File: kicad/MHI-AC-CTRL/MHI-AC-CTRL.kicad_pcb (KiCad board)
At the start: 2 copper layers, 51.6 x 26.8 mm, 8 parts, among them J1 Conn_01x05, U1 TSR_1-2450, U2 ESP-C3-32S-Kit, U3 LEVEL-SHIFTER-4CH

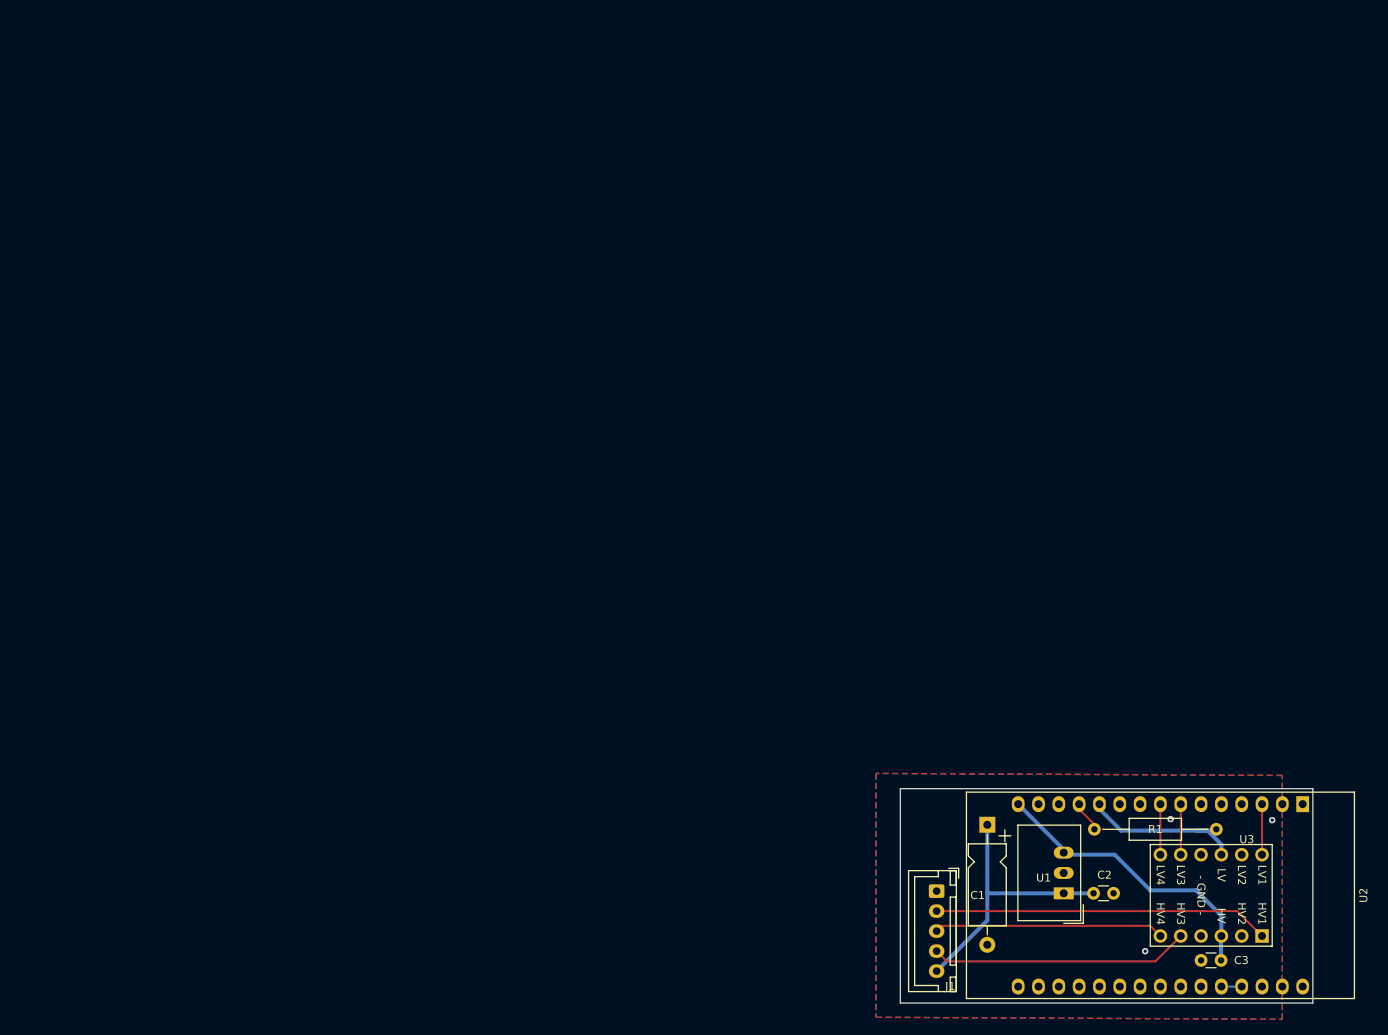
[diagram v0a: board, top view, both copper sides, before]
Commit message: Custom Version for ESP32-C3-DevkitM-1
Custom Version for ESP32-C3-DevkitM-1
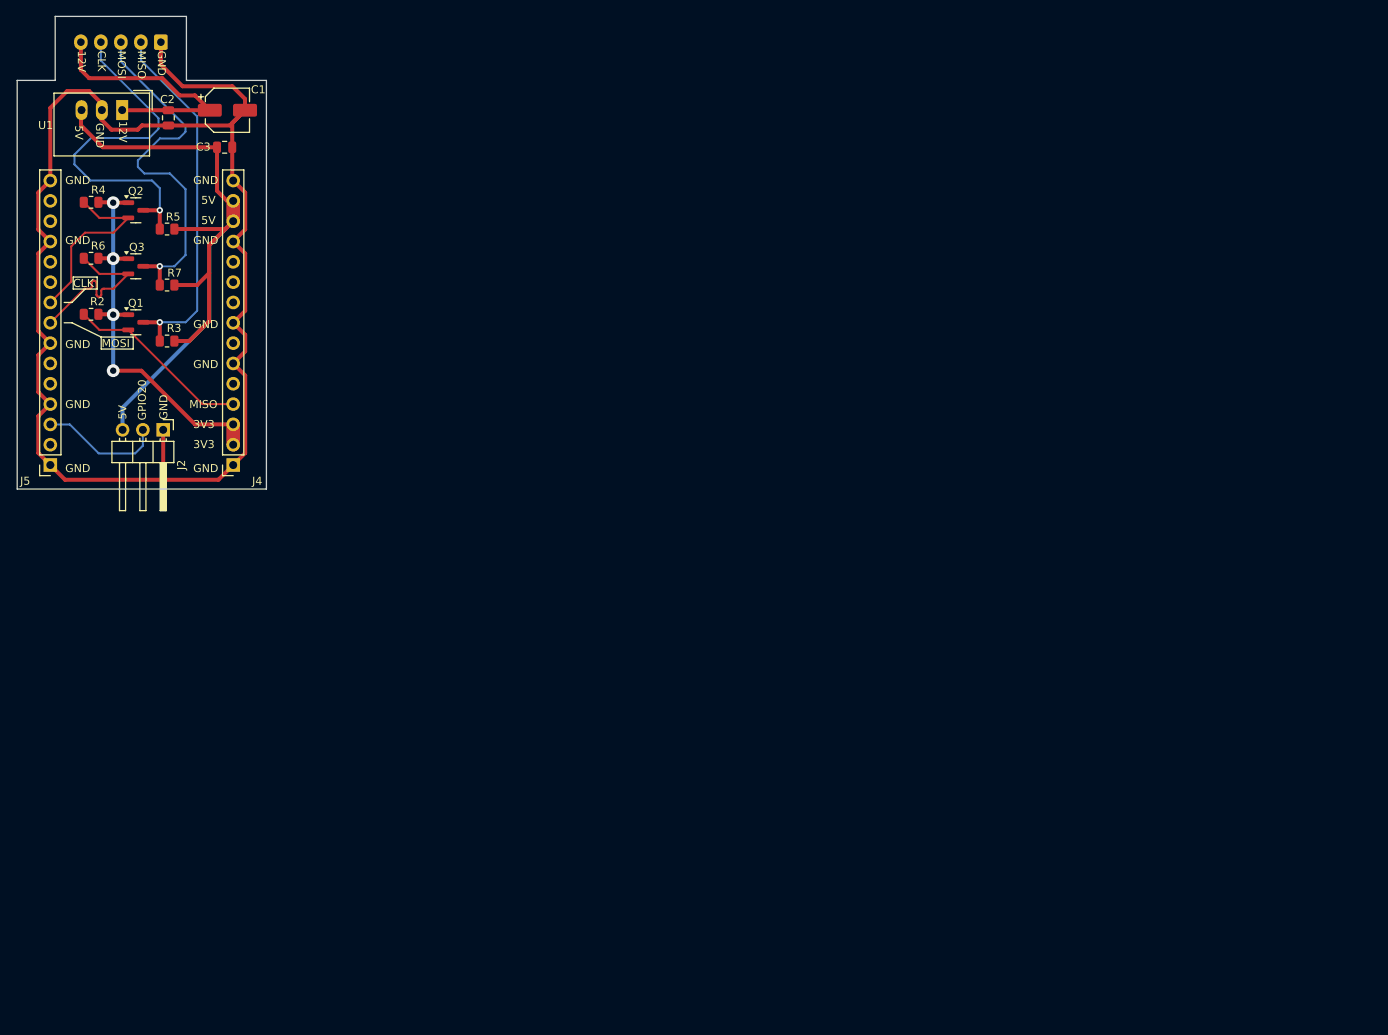
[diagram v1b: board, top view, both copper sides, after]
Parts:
- removed R1: 12K, Resistor_THT:R_Axial_DIN0207_L6.3mm_D2.5mm_P15.24mm_Horizontal
- removed U2: ESP-C3-32S-Kit, MHI-AC-CTRL:ESP-C3-32S-Kit
- removed U3: LEVEL-SHIFTER-4CH, Package_SO:SOIC-14_3.9x8.7mm_P1.27mm
- added J2: Conn_01x03_Pin, Connector_PinHeader_2.54mm:PinHeader_1x03_P2.54mm_Horizontal, F.Cu at (-15.4, -7.39)
- added J4: Conn_01x15_Socket, Connector_PinSocket_2.54mm:PinSocket_1x15_P2.54mm_Vertical, F.Cu at (-4.14, -2.99)
- added J5: Conn_01x15_Socket, Connector_PinSocket_2.54mm:PinSocket_1x15_P2.54mm_Vertical, F.Cu at (-27.0, -2.99)
- added Q1: BSS138, Package_TO_SOT_SMD:SOT-23, F.Cu at (-16.3, -20.8)
- added Q2: BSS138, Package_TO_SOT_SMD:SOT-23, F.Cu at (-16.3, -34.8)
- added Q3: BSS138, Package_TO_SOT_SMD:SOT-23, F.Cu at (-16.3, -27.8)
- added R2: 10K, Resistor_SMD:R_0805_2012Metric, F.Cu at (-21.9, -21.8)
- added R3: 10K, Resistor_SMD:R_0805_2012Metric, F.Cu at (-12.4, -18.5)
- added R4: 10K, Resistor_SMD:R_0805_2012Metric, F.Cu at (-21.9, -35.8)
- added R5: 10K, Resistor_SMD:R_0805_2012Metric, F.Cu at (-12.4, -32.5)
- added R6: 10K, Resistor_SMD:R_0805_2012Metric, F.Cu at (-21.9, -28.8)
- added R7: 10K, Resistor_SMD:R_0805_2012Metric, F.Cu at (-12.4, -25.5)
- C1: footprint Capacitor_THT:CP_Axial_L10.0mm_D4.5mm_P15.00mm_Horizontal -> Capacitor_SMD:CP_Elec_5x5.3
- C2, C3: footprint Capacitor_THT:C_Disc_D3.0mm_W1.6mm_P2.50mm -> Capacitor_SMD:C_0805_2012Metric
- J1: moved to B.Cu
- moved C3 160.8 mm to (-5.21, -42.7), turned to 0 degrees
- moved U1 153.9 mm to (-18.0, -48.6), turned to 180 degrees
- moved C2 150.9 mm to (-12.2, -46.4), turned to -90 degrees
- moved J1 143.8 mm to (-13.2, -55.8), turned to 180 degrees
- moved C1 130.4 mm to (-4.86, -47.3), turned to 180 degrees
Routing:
- net GND: track 0.00 -> 175.1 mm, vias 3 -> 0
- net +5V: track 37.1 -> 93.0 mm
- net +3V3: track 21.6 -> 52.6 mm, vias 0 -> 4
- net MOSI_5V: track 28.8 -> 46.4 mm, vias 0 -> 1
- net MISO_3V3: track 6.32 -> 23.3 mm
- net CLK_3V3: track 6.32 -> 23.1 mm
- net MOSI_3V3: track 6.32 -> 22.0 mm
- net Net-(J2-Pin_2): track 0.00 -> 15.5 mm
- net CLK_5V: track 32.4 -> 45.9 mm, vias 0 -> 1
- net Net-(U2-EN): track 5.17 -> 0.00 mm
- net MISO_5V: track 42.0 -> 46.1 mm, vias 0 -> 1
- net Net-(U2-IO10): track 2.54 -> 0.00 mm
- net +12V: track 34.2 -> 32.7 mm
- removed copper zone on B.Cu, net GND
- removed copper zone on F.Cu, net GND
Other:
- board size 51.6 x 26.8 mm -> 31.2 x 59.1 mm
- board text added: "12V"
- board text added: "3V3"
- board text added: "5V"
- board text added: "CLK"
- board text added: "GND"
- board text added: "GPIO20"
- board text added: "MHI AC Interface for ESP32-C3-DevKitM-1 Prototype v0.1"
- board text added: "MISO"
- board text added: "MOSI"
- board text removed: "MHI-AC-Ctrl-ESP32-C3 v1.0 January 2023"
